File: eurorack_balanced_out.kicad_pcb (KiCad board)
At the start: 2 copper layers, 80 x 40 mm, 31 parts, among them J1 Conn_01x02, J2 Conn_01x02, J3 Conn_02x05_Odd_Even, J4 AudioJack3, J5 AudioJack3, U1 THAT1646W16, U2 THAT1646W16

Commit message: rought first placement
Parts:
- moved C9 63.6 mm to (129.0, 123.0), turned to 180 degrees
- moved C11 62.1 mm to (149.0, 123.0)
- moved FB1 57.4 mm to (149.0, 127.0)
- moved FB2 56.0 mm to (129.0, 126.0), turned to 180 degrees
- moved C12 53.8 mm to (177.0, 123.0)
- moved C10 50.4 mm to (157.0, 123.0), turned to 180 degrees
- moved FB3 43.8 mm to (177.0, 127.0)
- moved FB4 39.5 mm to (157.0, 127.0), turned to 180 degrees
- moved J1 38.5 mm to (142.0, 148.0), turned to 90 degrees
- moved R1 31.4 mm to (138.0, 148.0)
- moved C6 31.0 mm to (130.0, 140.0)
- moved D3 30.1 mm to (149.0, 132.0), turned to 180 degrees
- moved U1 29.0 mm to (139.0, 139.0)
- moved C5 26.0 mm to (148.0, 140.0)
- moved R3 23.1 mm to (134.0, 148.0)
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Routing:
- added copper zone on B.Cu, net GND
- added copper zone on F.Cu, net GND

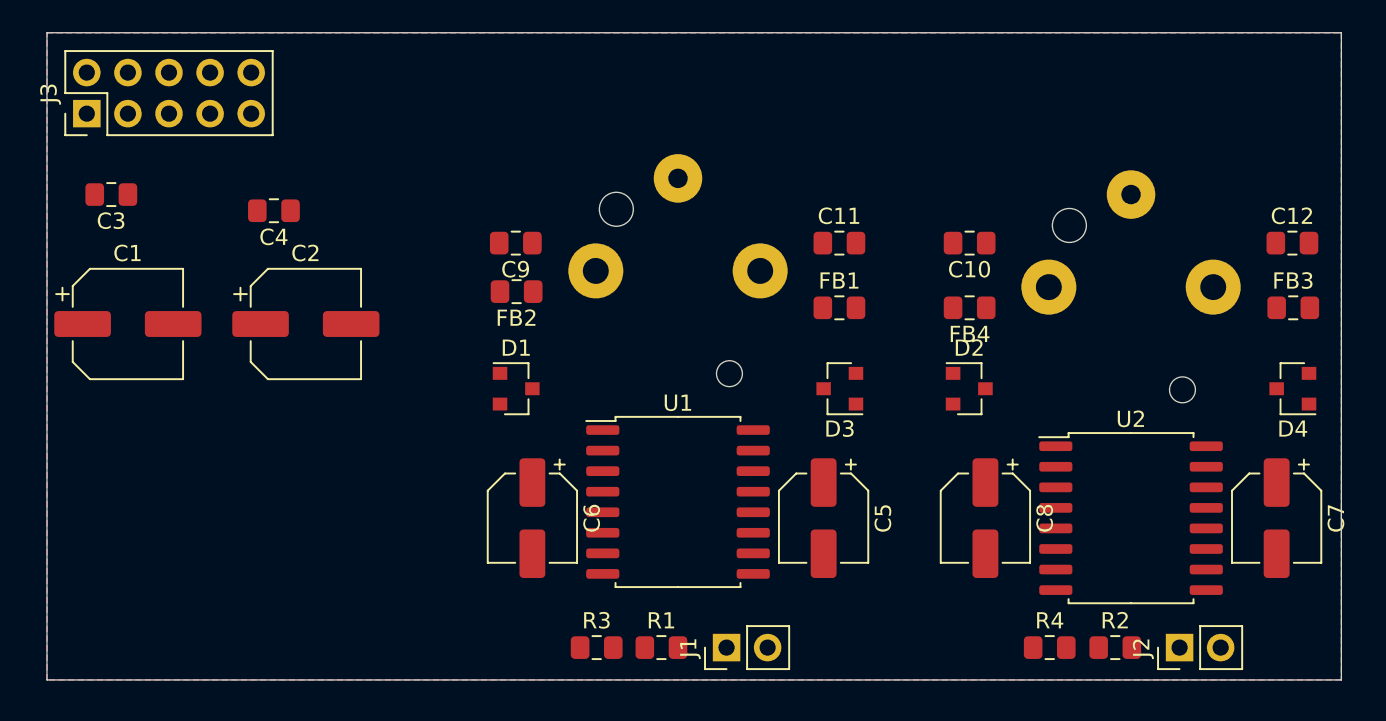
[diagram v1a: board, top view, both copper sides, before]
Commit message: try to make placement a bit more compact
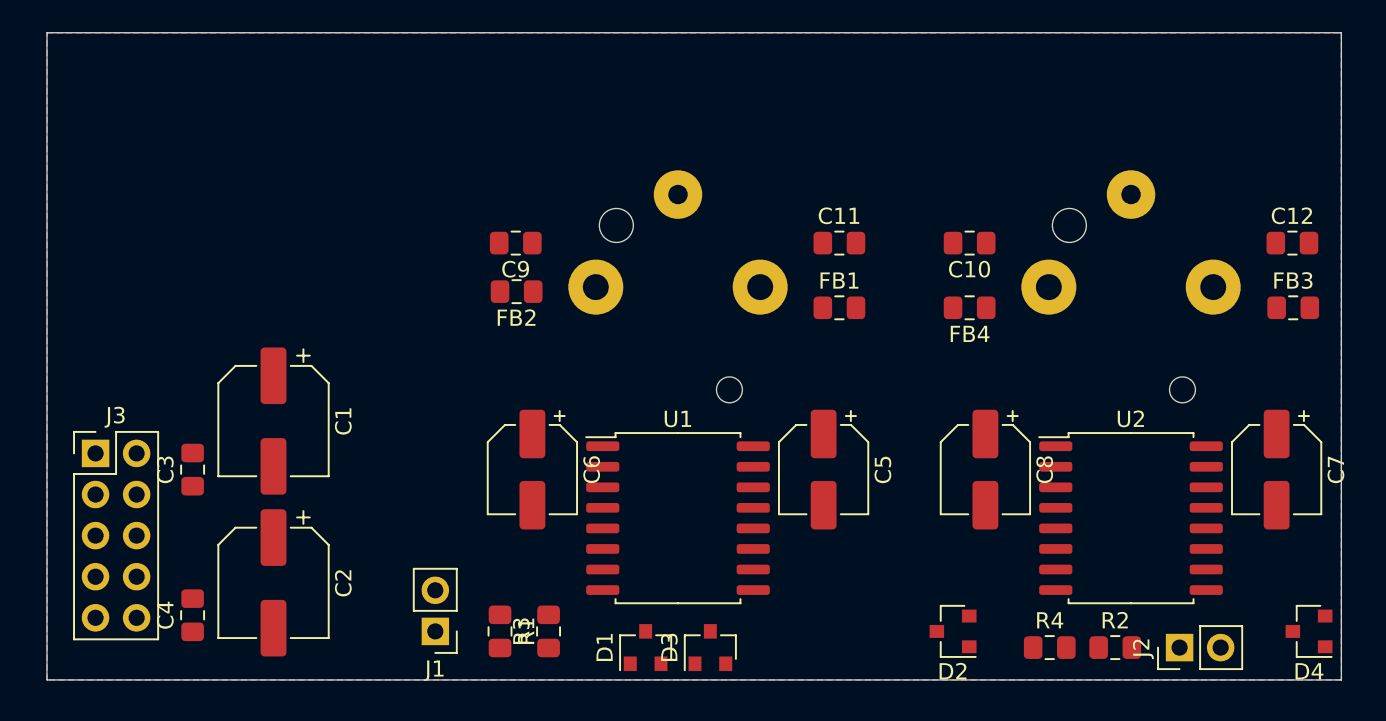
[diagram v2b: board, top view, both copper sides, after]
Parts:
- moved C4 25.5 mm to (109.0, 146.0), turned to 90 degrees
- moved J3 21.0 mm to (103.0, 136.0), turned to 0 degrees
- moved J1 18.0 mm to (124.0, 147.0), turned to 180 degrees
- moved D1 17.9 mm to (137.0, 148.0), turned to 90 degrees
- moved D3 17.9 mm to (141.0, 148.0), turned to 90 degrees
- moved C3 17.7 mm to (109.0, 137.0), turned to 90 degrees
- moved C2 16.1 mm to (114.0, 144.0), turned to 270 degrees
- moved D2 15.0 mm to (156.0, 147.0), turned to 180 degrees
- moved D4 15.0 mm to (178.0, 147.0)
- moved C1 10.8 mm to (114.0, 134.0), turned to 270 degrees
- moved R1 10.0 mm to (128.0, 147.0), turned to 270 degrees
- moved R3 3.14 mm to (131.0, 147.0), turned to 90 degrees
- moved C5 3.00 mm to (148.0, 137.0)
- moved C6 3.00 mm to (130.0, 137.0)
- moved C7 3.00 mm to (176.0, 137.0)
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
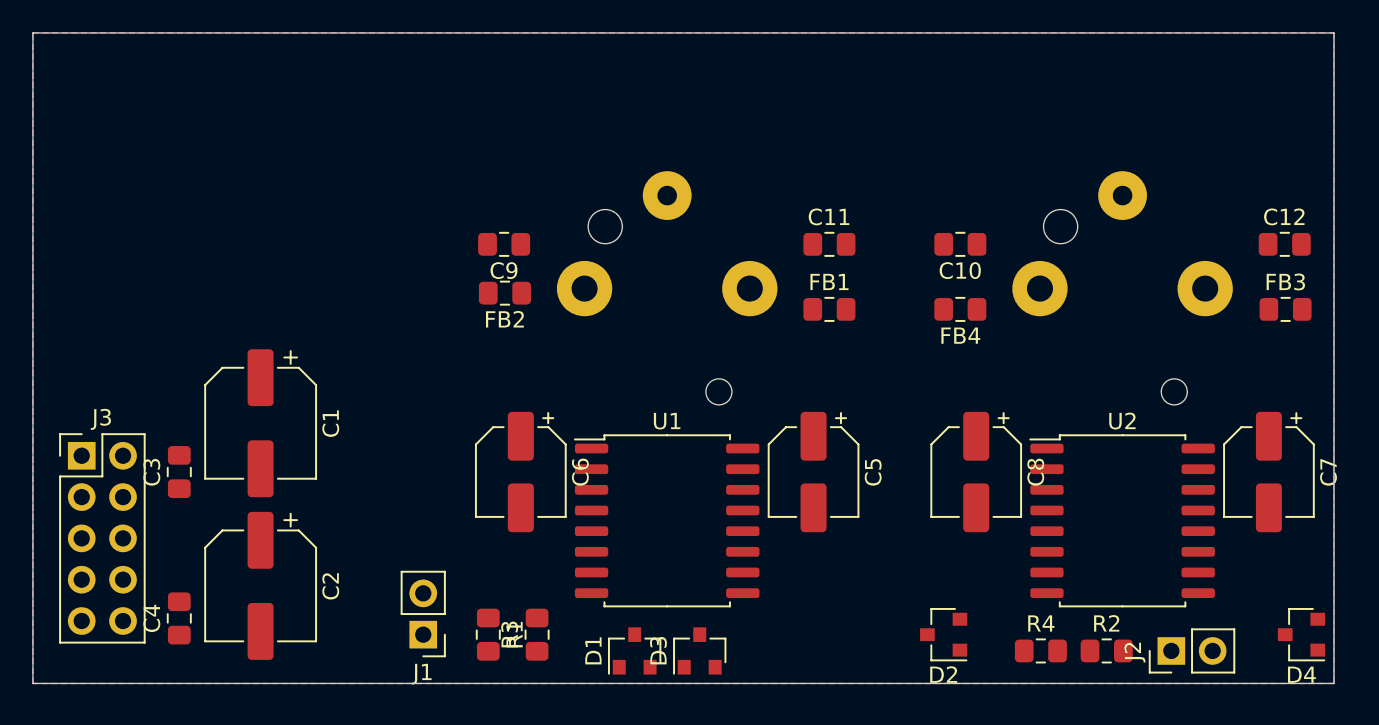
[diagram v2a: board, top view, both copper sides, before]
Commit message: save some more board space
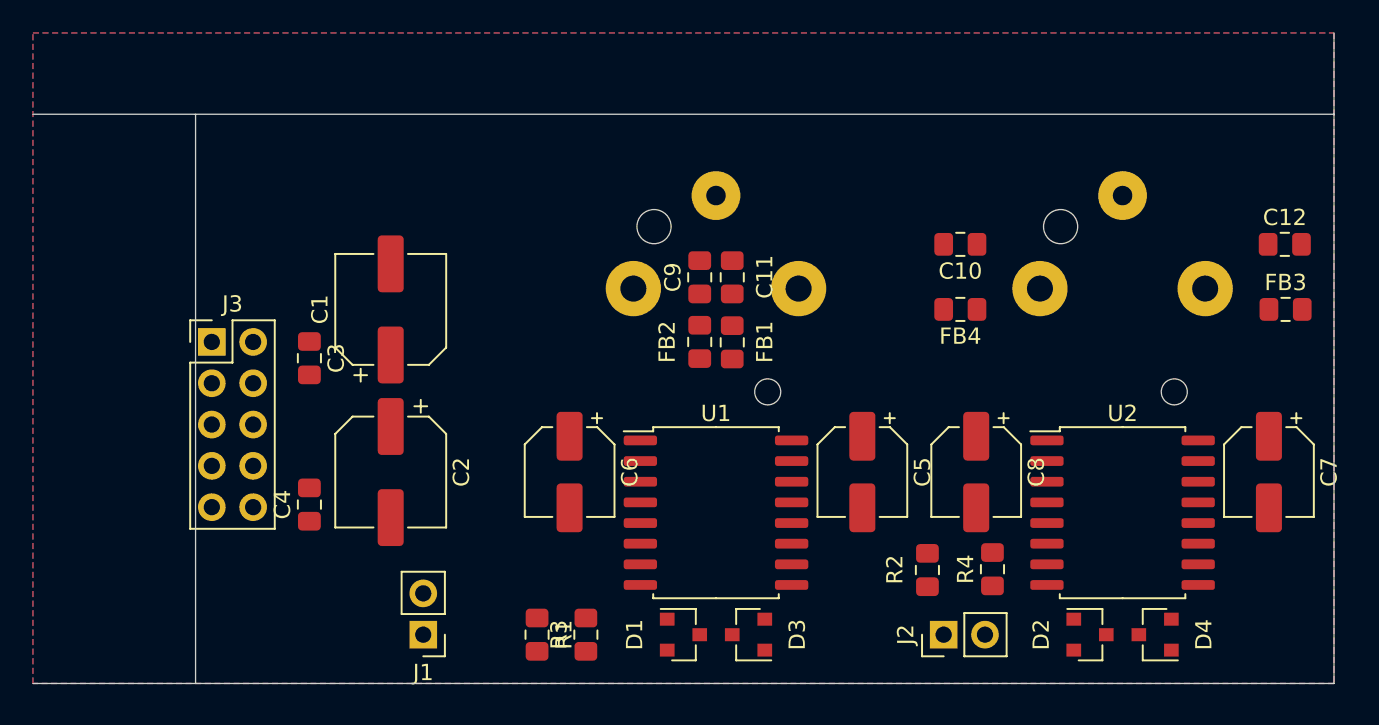
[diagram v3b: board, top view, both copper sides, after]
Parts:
- moved J2 14.0 mm to (156.0, 147.0)
- moved FB2 12.3 mm to (141.0, 129.0), turned to 270 degrees
- moved C9 12.2 mm to (141.0, 125.0), turned to 90 degrees
- moved R2 12.1 mm to (155.0, 143.0), turned to 270 degrees
- moved C1 10.6 mm to (122.0, 127.0), turned to 90 degrees
- moved C2 10.6 mm to (122.0, 137.0)
- moved C3 10.6 mm to (117.0, 130.0), turned to 270 degrees
- moved C4 10.6 mm to (117.0, 139.0)
- moved J3 10.6 mm to (111.0, 129.0)
- moved D2 9.00 mm to (165.0, 147.0), turned to 0 degrees
- moved D4 9.00 mm to (169.0, 147.0)
- moved C11 6.31 mm to (143.0, 125.0), turned to 90 degrees
- moved FB1 6.31 mm to (143.0, 129.0), turned to 270 degrees
- moved R4 5.84 mm to (159.0, 143.0), turned to 90 degrees
- moved D1 3.16 mm to (140.0, 147.0), turned to 0 degrees
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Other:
- outline, holes or cut-outs redrawn

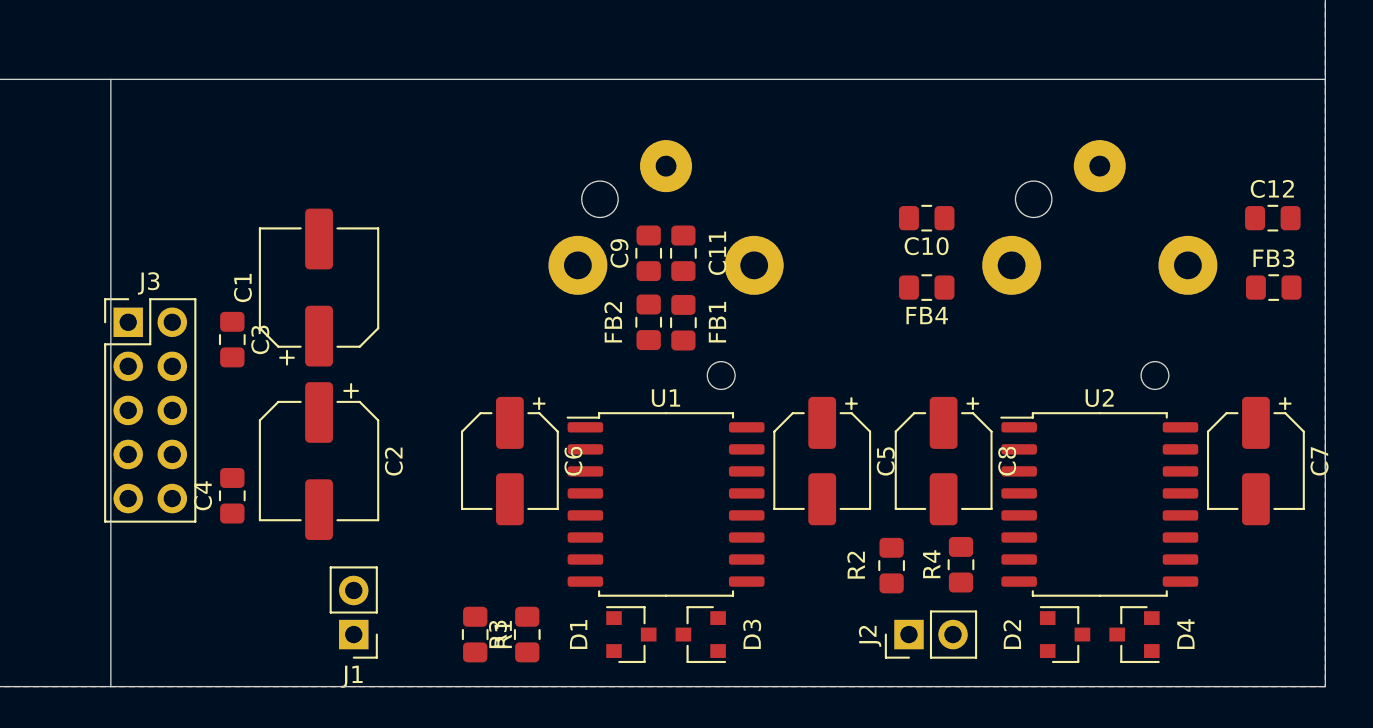
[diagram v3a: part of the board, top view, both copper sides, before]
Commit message: clean up component placement
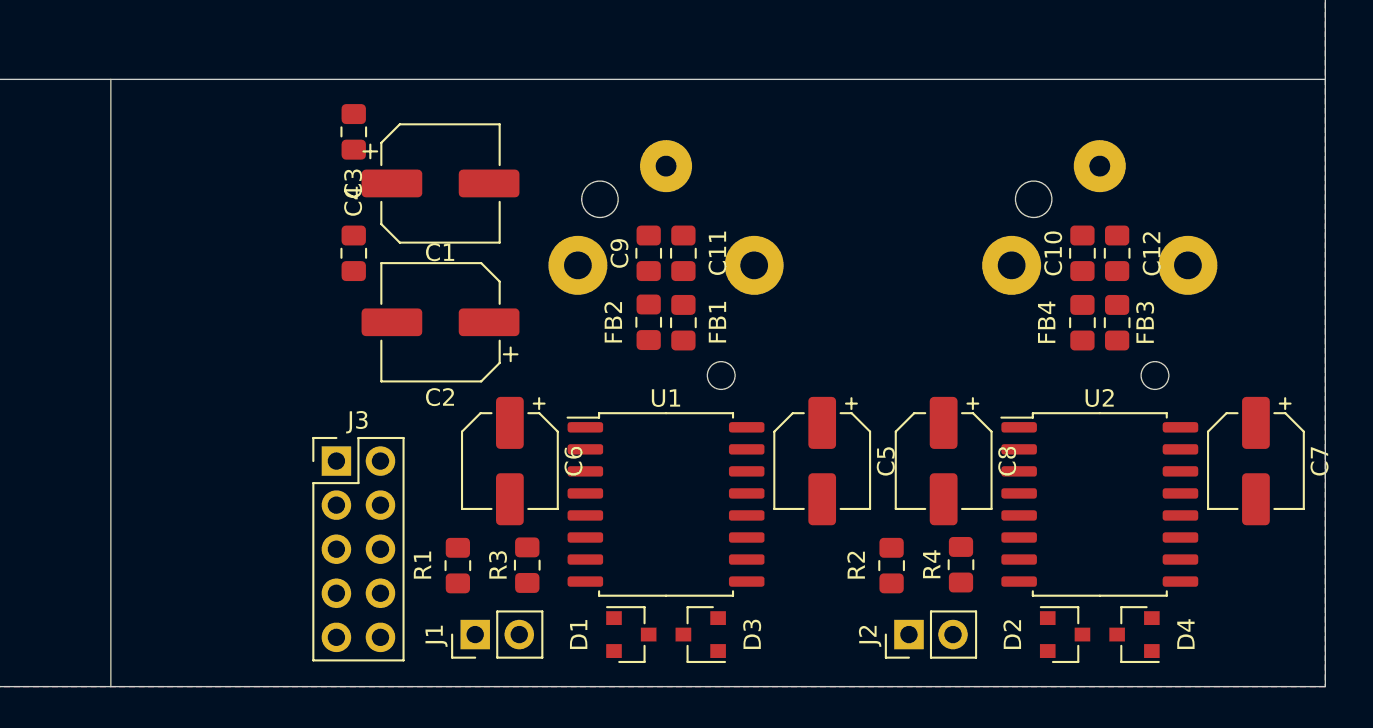
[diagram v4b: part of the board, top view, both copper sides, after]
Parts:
- moved C4 15.6 mm to (124.0, 125.0)
- moved J3 14.4 mm to (123.0, 137.0)
- moved C3 13.9 mm to (124.0, 118.0), turned to 90 degrees
- moved C2 10.6 mm to (129.0, 129.0), turned to 180 degrees
- moved FB3 9.25 mm to (168.0, 129.0), turned to 270 degrees
- moved C1 9.22 mm to (129.0, 121.0), turned to 0 degrees
- moved C10 9.20 mm to (166.0, 125.0), turned to 90 degrees
- moved C12 9.20 mm to (168.0, 125.0), turned to 90 degrees
- moved FB4 9.20 mm to (166.0, 129.0), turned to 270 degrees
- moved J1 7.00 mm to (131.0, 147.0), turned to 90 degrees
- moved R1 4.10 mm to (130.0, 143.0)
- moved R3 4.00 mm to (134.0, 143.0)

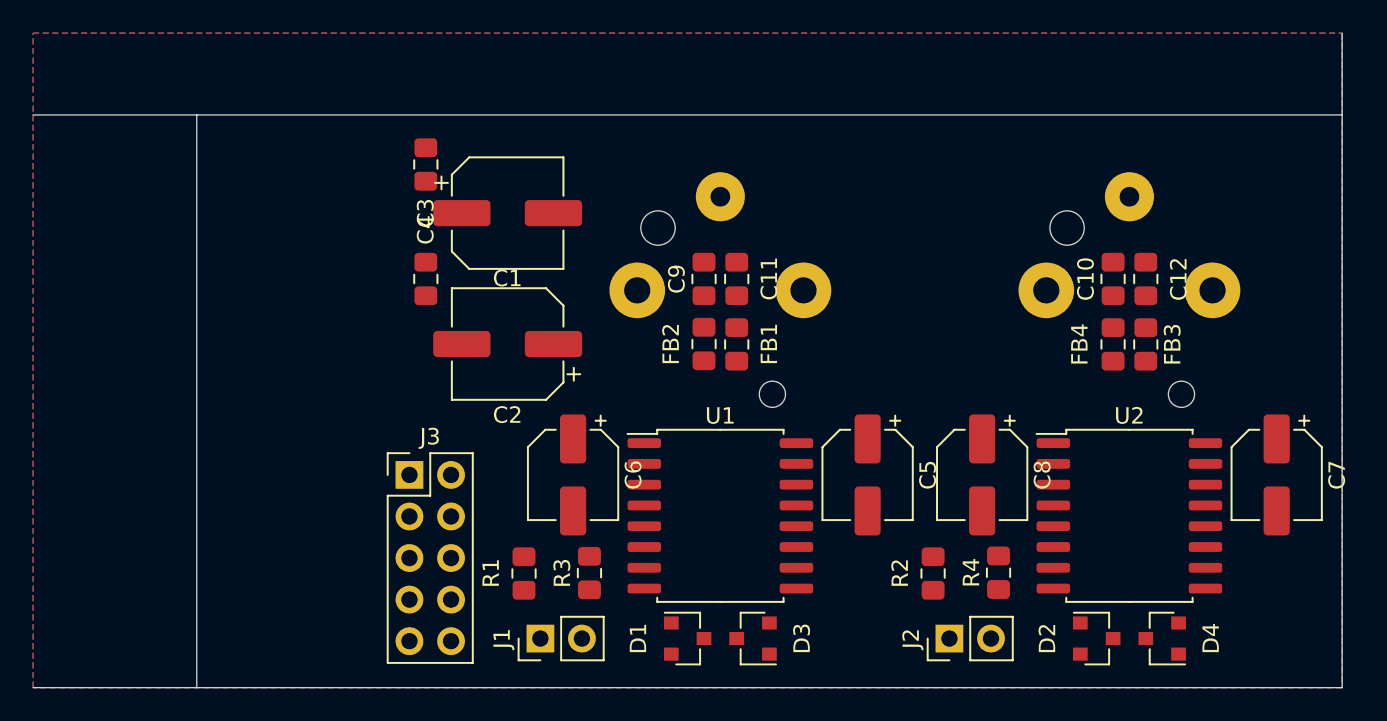
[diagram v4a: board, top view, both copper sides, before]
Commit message: clean up edgecut
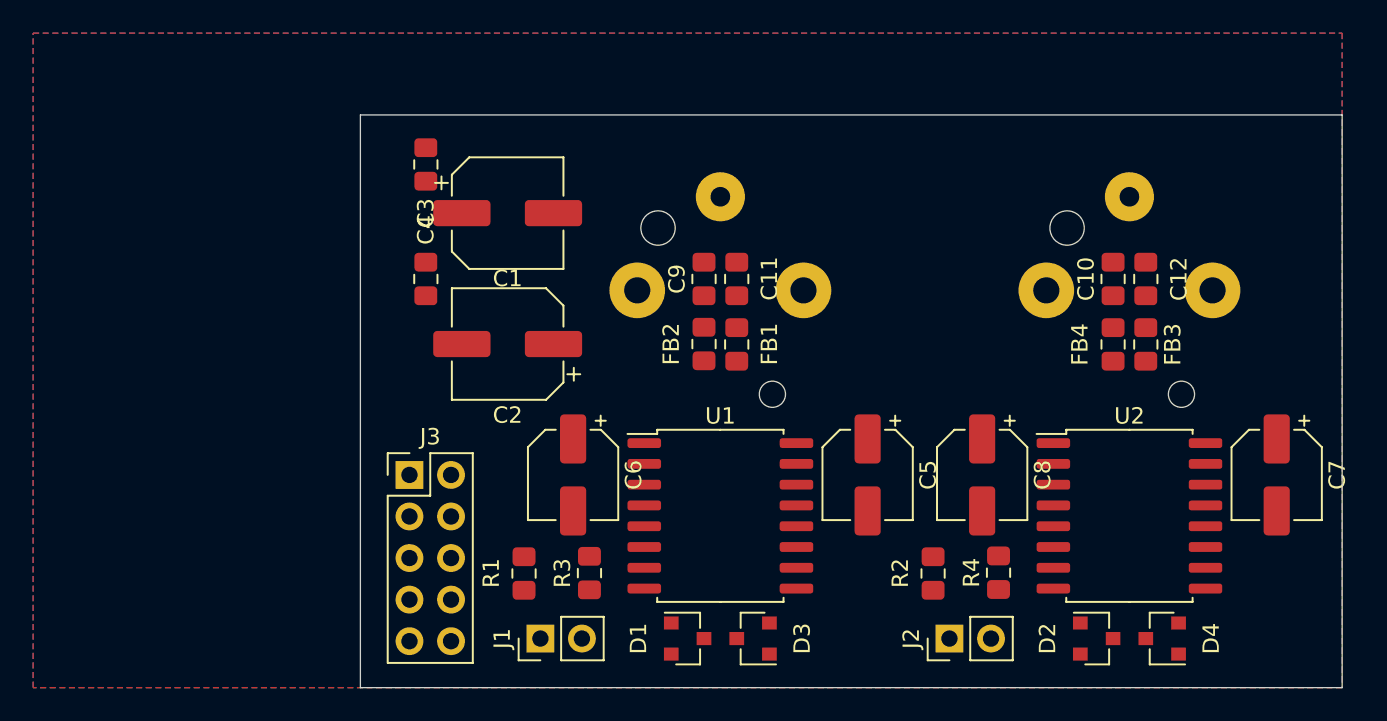
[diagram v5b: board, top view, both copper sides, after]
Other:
- board size 80 x 40 mm -> 60 x 35 mm
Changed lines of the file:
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@@
     )
   )
-  (gr_line (start 110 115) (end 110 150) (layer Edge.Cuts) (width 0.05))
-  (gr_line (start 100 115) (end 180 115) (layer Edge.Cuts) (width 0.05))
-  (gr_line (start 180 150) (end 100 150) (layer Edge.Cuts) (width 0.05))
-  (gr_line (start 180 110) (end 180 150) (layer Edge.Cuts) (width 0.05))
+  (gr_line (start 120 115) (end 120 150) (layer Edge.Cuts) (width 0.05))
+  (gr_line (start 120 115) (end 180 115) (layer Edge.Cuts) (width 0.05))
+  (gr_line (start 180 150) (end 120 150) (layer Edge.Cuts) (width 0.05))
+  (gr_line (start 180 115) (end 180 150) (layer Edge.Cuts) (width 0.05))
   (zone (net 1) (net_name GND) (layer F.Cu) (hatch edge 0.508)
     (connect_pads (clearance 0.508))

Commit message: route signals and some power
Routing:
- net Net-(C6-Pad1): track 0.00 -> 27.0 mm
- net Net-(C8-Pad1): track 0.00 -> 26.9 mm
- net Net-(C7-Pad1): track 0.00 -> 26.9 mm
- net Net-(C5-Pad1): track 0.00 -> 26.3 mm
- net Vcc: track 0.00 -> 22.2 mm, vias 0 -> 5
- net Vee: track 0.00 -> 15.3 mm, vias 0 -> 5
- net Net-(C12-Pad1): track 0.00 -> 9.78 mm
- net Net-(C11-Pad1): track 0.00 -> 9.78 mm
- net Net-(R2-Pad1): track 0.00 -> 7.60 mm
- net Net-(R1-Pad1): track 0.00 -> 7.60 mm
- net Net-(C10-Pad1): track 0.00 -> 6.17 mm
- net Net-(C9-Pad1): track 0.00 -> 6.14 mm
- net Net-(C8-Pad2): track 0.00 -> 4.49 mm
- net Net-(C7-Pad2): track 0.00 -> 4.49 mm
- net Net-(C6-Pad2): track 0.00 -> 4.49 mm
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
